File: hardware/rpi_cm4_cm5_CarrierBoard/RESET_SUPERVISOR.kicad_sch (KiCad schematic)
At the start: 34 parts, among them Q13 2N7002, Q8 2N7002, Q9 2N7002, U30 STM6710DWB6F, U31 SN74LVC1G125DBVR, U32 SN74HCS365QPWRQ1, U35 SN74HCS365QPWRQ1

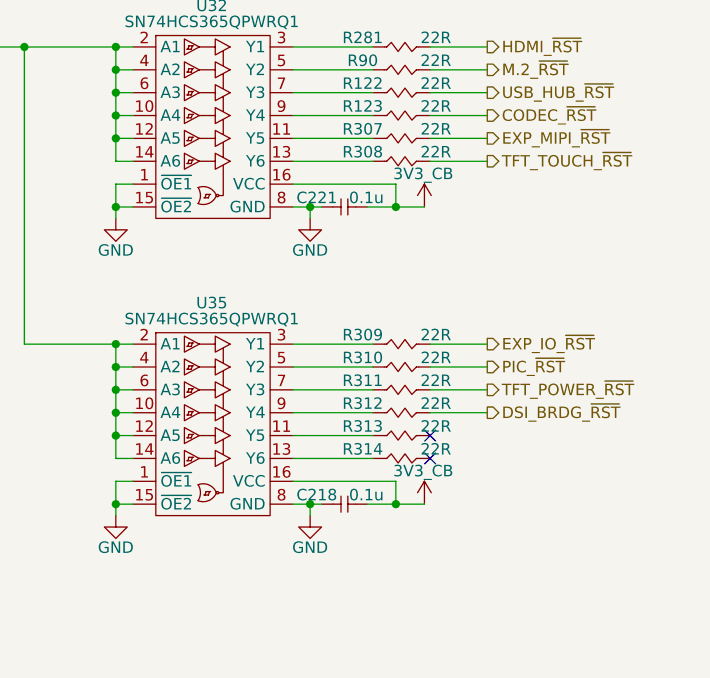
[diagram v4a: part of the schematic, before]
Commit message: Review watchdog timer circuit to prevent race condition during shutdown
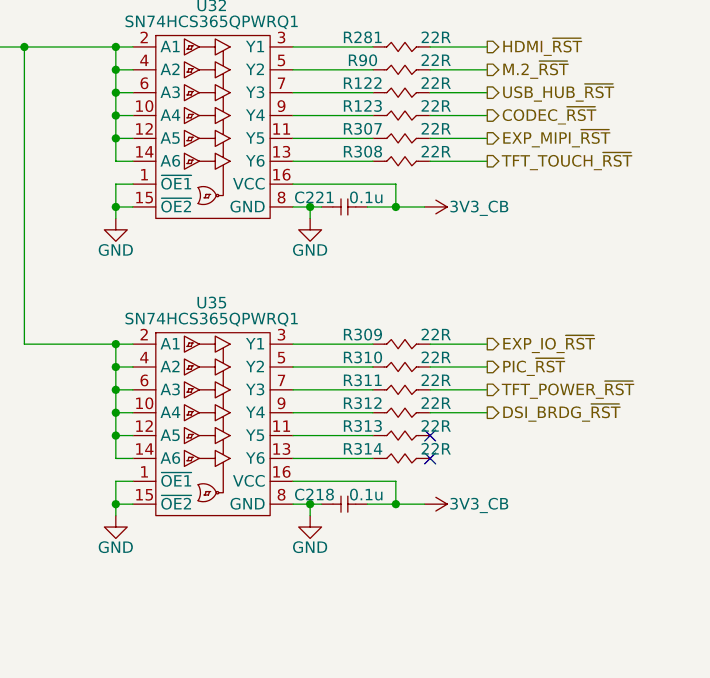
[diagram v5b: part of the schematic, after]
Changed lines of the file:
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@@
 			)
 		)
-		(column_widths 12.065 11.43 8.255)
+		(column_widths 12.065 11.43 11.43)
 		(row_heights 2.54 2.54 2.54 2.54 2.54)
 		(cells
 			(table_cell "PER_~{RST}"
 				(exclude_from_sim no)
-				(at 139.065 132.08 0)
+				(at 137.16 132.08 0)
 				(size 12.065 2.54)
 				(margins 0.9525 0.9525 0.9525 0.9525)
@@
 			(table_cell "EXT_~{RST}"
 				(exclude_from_sim no)
-				(at 151.13 132.08 0)
+				(at 149.225 132.08 0)
 				(size 11.43 2.54)
 				(margins 0.9525 0.9525 0.9525 0.9525)
@@
 			(table_cell "PWG"
 				(exclude_from_sim no)
-				(at 162.56 132.08 0)
-				(size 8.255 2.54)
+				(at 160.655 132.08 0)
+				(size 11.43 2.54)
 				(margins 0.9525 0.9525 0.9525 0.9525)
 				(span 1 1)
@@
 			(table_cell "0"
 				(exclude_from_sim no)
-				(at 139.065 134.62 0)
+				(at 137.16 134.62 0)
 				(size 12.065 2.54)
 				(margins 0.9525 0.9525 0.9525 0.9525)
@@
 			(table_cell "0"
 				(exclude_from_sim no)
-				(at 151.13 134.62 0)
+				(at 149.225 134.62 0)
 				(size 11.43 2.54)
 				(margins 0.9525 0.9525 0.9525 0.9525)
@@
 			(table_cell "0"
 				(exclude_from_sim no)
-				(at 162.56 134.62 0)
-				(size 8.255 2.54)
+				(at 160.655 134.62 0)
+				(size 11.43 2.54)
 				(margins 0.9525 0.9525 0.9525 0.9525)
 				(span 1 1)
@@
 			(table_cell "0"
 				(exclude_from_sim no)
-				(at 139.065 137.16 0)
+				(at 137.16 137.16 0)
 				(size 12.065 2.54)
 				(margins 0.9525 0.9525 0.9525 0.9525)
@@
 			(table_cell "0"
 				(exclude_from_sim no)
-				(at 151.13 137.16 0)
+				(at 149.225 137.16 0)
 				(size 11.43 2.54)
 				(margins 0.9525 0.9525 0.9525 0.9525)
@@
 			(table_cell "1"
 				(exclude_from_sim no)
-				(at 162.56 137.16 0)
-				(size 8.255 2.54)
+				(at 160.655 137.16 0)
+				(size 11.43 2.54)
 				(margins 0.9525 0.9525 0.9525 0.9525)
 				(span 1 1)
@@
 			(table_cell "0"
 				(exclude_from_sim no)
-				(at 139.065 139.7 0)
+				(at 137.16 139.7 0)
 				(size 12.065 2.54)
 				(margins 0.9525 0.9525 0.9525 0.9525)
@@
 			(table_cell "1"
 				(exclude_from_sim no)
-				(at 151.13 139.7 0)
+				(at 149.225 139.7 0)
 				(size 11.43 2.54)
 				(margins 0.9525 0.9525 0.9525 0.9525)
@@
 			(table_cell "0"
 				(exclude_from_sim no)
-				(at 162.56 139.7 0)
-				(size 8.255 2.54)
+				(at 160.655 139.7 0)
+				(size 11.43 2.54)
 				(margins 0.9525 0.9525 0.9525 0.9525)
 				(span 1 1)
@@
 			(table_cell "1"
 				(exclude_from_sim no)
-				(at 139.065 142.24 0)
+				(at 137.16 142.24 0)
 				(size 12.065 2.54)
 				(margins 0.9525 0.9525 0.9525 0.9525)
@@
 			(table_cell "1"
 				(exclude_from_sim no)
-				(at 151.13 142.24 0)
+				(at 149.225 142.24 0)
 				(size 11.43 2.54)
 				(margins 0.9525 0.9525 0.9525 0.9525)
@@
 			(table_cell "1"
 				(exclude_from_sim no)
-				(at 162.56 142.24 0)
-				(size 8.255 2.54)
+				(at 160.655 142.24 0)
+				(size 11.43 2.54)
 				(margins 0.9525 0.9525 0.9525 0.9525)
 				(span 1 1)
@@
 	(symbol
 		(lib_id "KiCad_Pwr_Symbols:+1V8")
-		(at 222.25 107.95 0)
-		(mirror y)
+		(at 222.25 107.95 270)
+		(mirror x)
 		(unit 1)
 		(exclude_from_sim no)
@@
 		(dnp no)
 		(property "Reference" "#PWR0326"
-			(at 222.25 111.76 0)
+			(at 218.44 107.95 0)
 			(effects
 				(font
@@
 		)
 		(property "Value" "3V3_CB"
-			(at 222.123 104.267 0)
+			(at 228.346 107.95 90)
 			(effects
 				(font
@@
 		(dnp no)
 		(property "Reference" "C221"
-			(at 208.026 106.934 0)
+			(at 207.772 106.934 0)
 			(effects
 				(font
@@
 	(symbol
 		(lib_id "KiCad_Pwr_Symbols:+1V8")
-		(at 222.25 140.97 0)
-		(mirror y)
+		(at 222.25 140.97 270)
+		(mirror x)
 		(unit 1)
 		(exclude_from_sim no)
@@
 		(dnp no)
 		(property "Reference" "#PWR0351"
-			(at 222.25 144.78 0)
+			(at 218.44 140.97 0)
 			(effects
 				(font
@@
 		)
 		(property "Value" "3V3_CB"
-			(at 222.123 137.287 0)
+			(at 228.346 140.97 90)
 			(effects
 				(font
@@
 		(dnp no)
 		(property "Reference" "C218"
-			(at 208.026 139.954 0)
+			(at 207.772 139.954 0)
 			(effects
 				(font

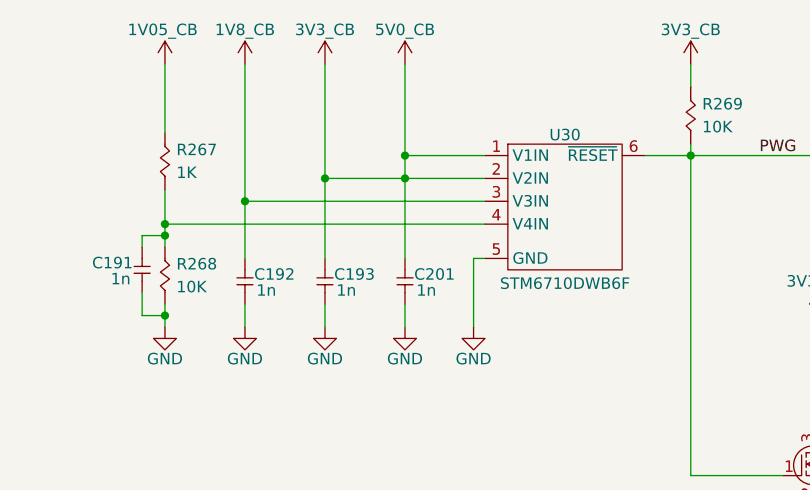
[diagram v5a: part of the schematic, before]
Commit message: Update preliminary placement, update DNP, regen BOM + Preliminary schematics
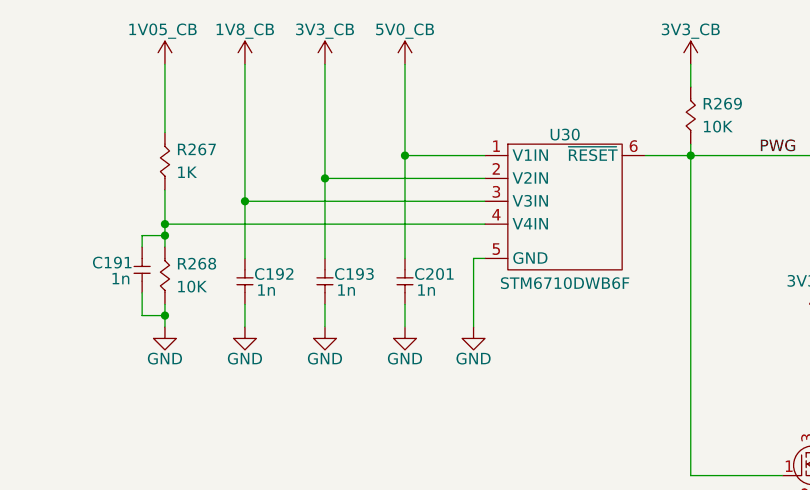
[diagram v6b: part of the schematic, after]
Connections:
- net 3V3_CB: no longer C201.2, U30.1 (V1IN)
- new net 5V0_CB: C201.2, U30.1 (V1IN)
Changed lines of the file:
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@@
-	)
-	(junction
-		(at 94.615 64.77)
-		(diameter 0)
-		(color 0 0 0 0)
 	)
 	(junction
@@
 	(wire
 		(pts
-			(xy 94.615 62.23) (xy 94.615 64.77)
-		)
-		(stroke
-			(width 0)
-			(type default)
-		)
-	)
-	(wire
-		(pts
-			(xy 94.615 64.77) (xy 103.505 64.77)
+			(xy 94.615 62.23) (xy 94.615 73.66)
+		)
+		(stroke
+			(width 0)
+			(type default)
+		)
+	)
+	(wire
+		(pts
+			(xy 85.725 64.77) (xy 103.505 64.77)
 		)
 		(stroke
@@
 	(wire
 		(pts
-			(xy 85.725 64.77) (xy 94.615 64.77)
-		)
-		(stroke
-			(width 0)
-			(type default)
-		)
-	)
-	(wire
-		(pts
 			(xy 187.96 102.87) (xy 189.865 102.87)
 		)
@@
 		)
 		(stroke
-			(width 0)
-			(type default)
-		)
-	)
-	(wire
-		(pts
-			(xy 94.615 64.77) (xy 94.615 73.66)
-		)
-		(stroke

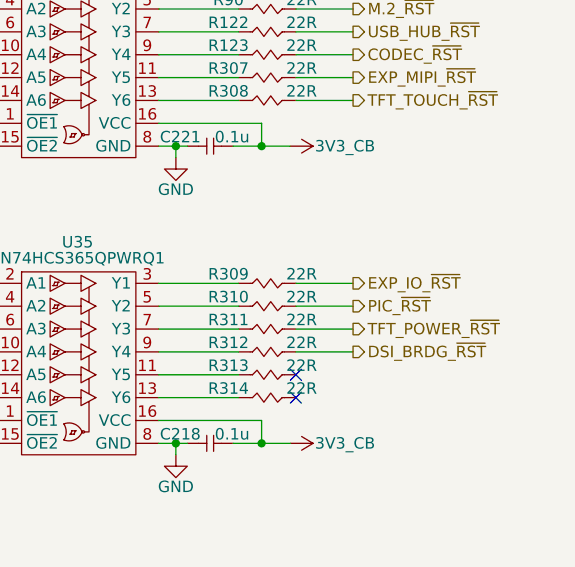
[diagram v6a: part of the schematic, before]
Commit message: Update PCB design rules for outer layers differential pairs Update preliminary component placement Update schematics based on PCB placement & remove duplicata / unnecessary components Update design notes and power table
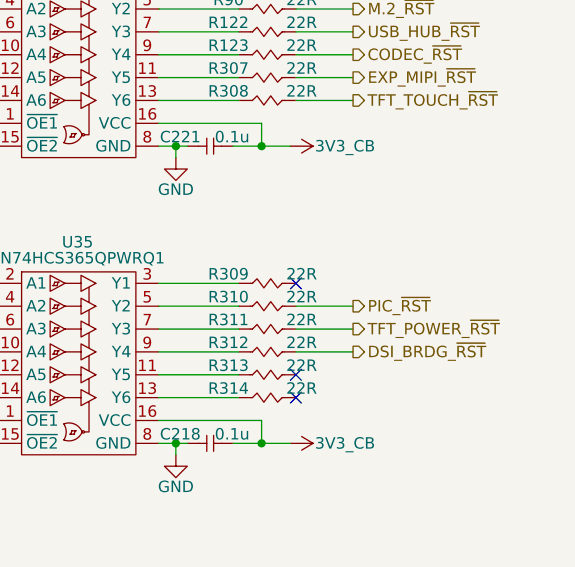
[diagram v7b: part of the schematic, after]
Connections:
- net EXP_IO_~{RST}: no longer names the net of R309.2
- no-connect marks 2 -> 3
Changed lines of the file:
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@@
 		(at 222.885 135.89)
 	)
+	(no_connect
+		(at 222.885 123.19)
+	)
 	(wire
 		(pts
@@
 		(pts
 			(xy 136.525 116.84) (xy 126.365 116.84)
-		)
-		(stroke
-			(width 0)
-			(type default)
-		)
-	)
-	(wire
-		(pts
-			(xy 222.885 123.19) (xy 229.235 123.19)
 		)
 		(stroke
@@
 		(effects
 			(font
-				(size 1.27 1.27)
-			)
-			(justify left)
-		)
-	)
-	(hierarchical_label "EXP_IO_~{RST}"
-		(shape output)
-		(at 229.235 123.19 0)
-		(effects
-			(font
